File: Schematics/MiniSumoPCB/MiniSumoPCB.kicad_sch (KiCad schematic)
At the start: 46 parts, among them J1 Alimentacion, J18 Servo, J2 AUX_12, J3 MOTOR_A, J4 MOTOR_B, J5 UART, J6 Micro_SD_Card, J8 POWER_OUT_1, Q1 IRLR8726, Q2 IRLM2502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

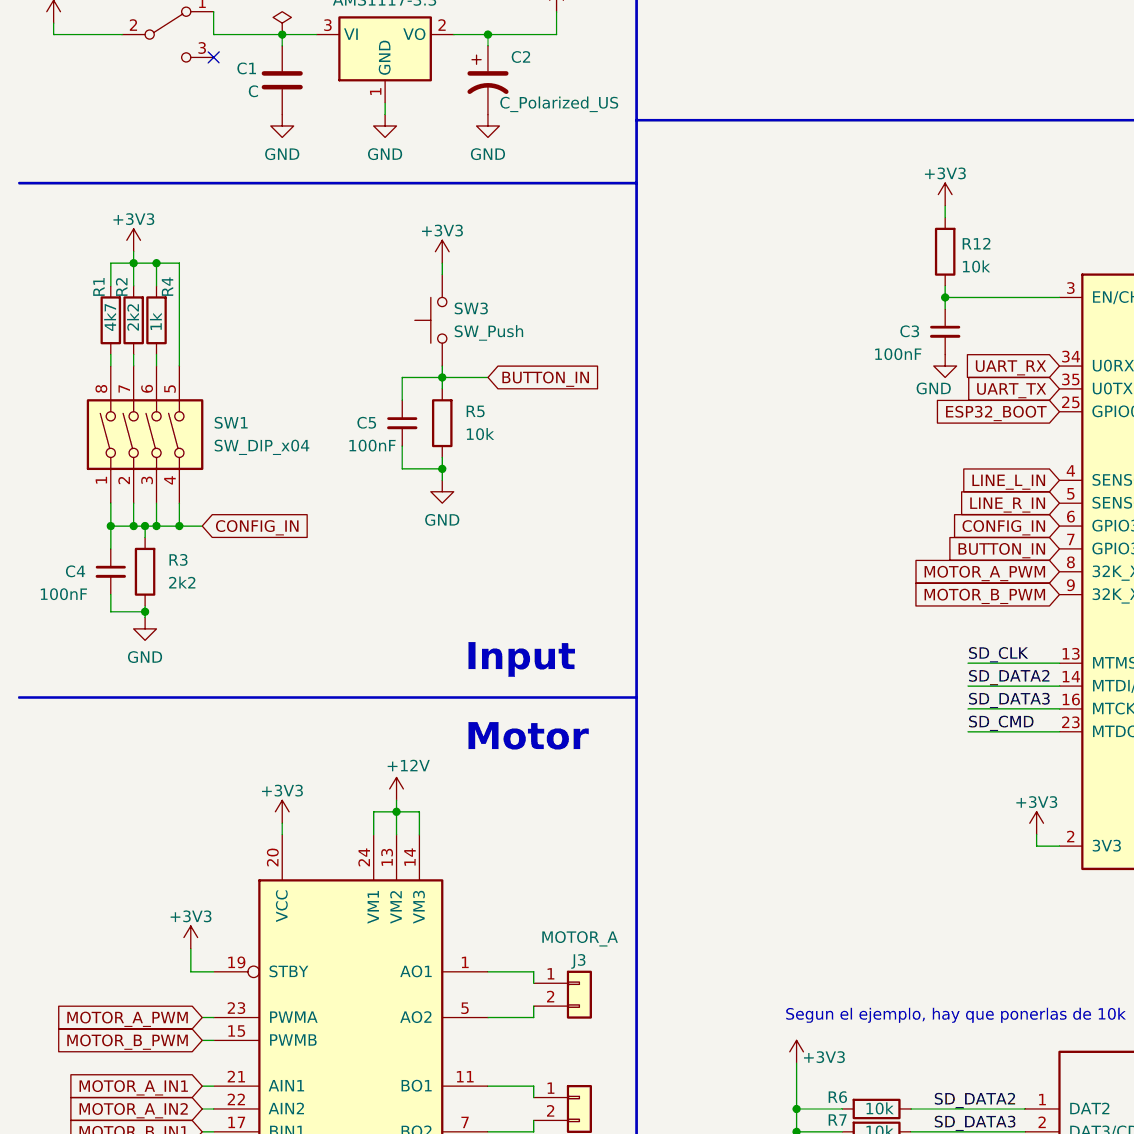
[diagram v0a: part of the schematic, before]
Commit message: [PCB] Added decoupling Capacitors
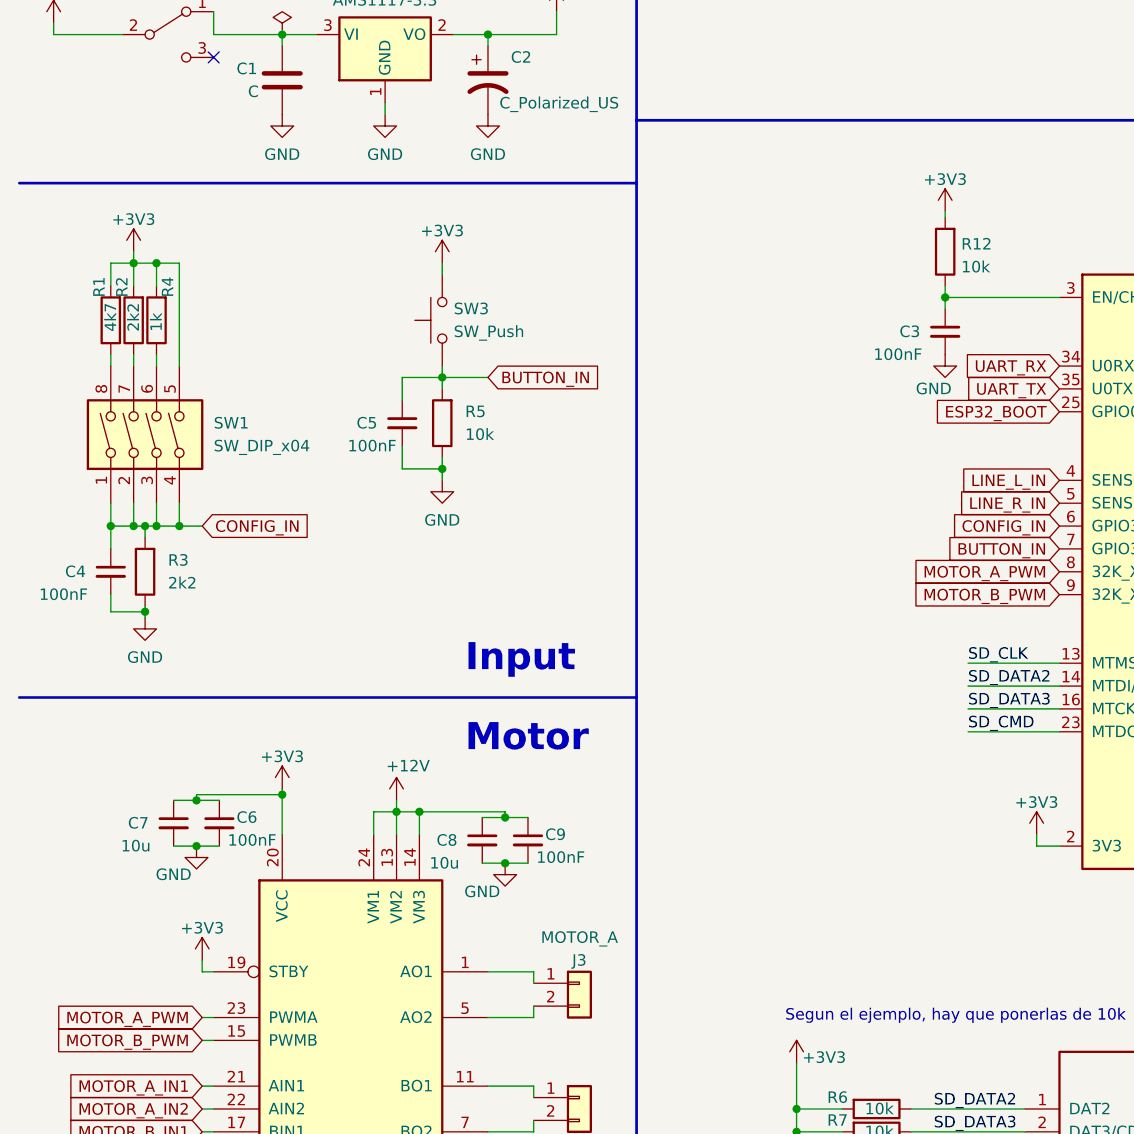
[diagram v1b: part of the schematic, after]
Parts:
- added C6, C9: 100nF, Capacitor_SMD:C_1206_3216Metric_Pad1.33x1.80mm_HandSolder, symbol Device:C_Small
- added C7, C8: 10u, Capacitor_SMD:C_1206_3216Metric_Pad1.33x1.80mm_HandSolder, symbol Device:C_Small
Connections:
- net +12V: now also C8.1, C9.1
- net +3V3: now also C6.1, C7.1
- net GND: now also C6.2, C7.2, C8.2, C9.2
